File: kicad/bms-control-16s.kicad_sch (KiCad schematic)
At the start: 39 parts, among them J1 MicroFit 2x7, J10 Conn_01x06, J2 UEXT, J3 USB_B_Micro, J4 Conn_01x06, J5 MicroFit 2x9, J9 Conn_01x06

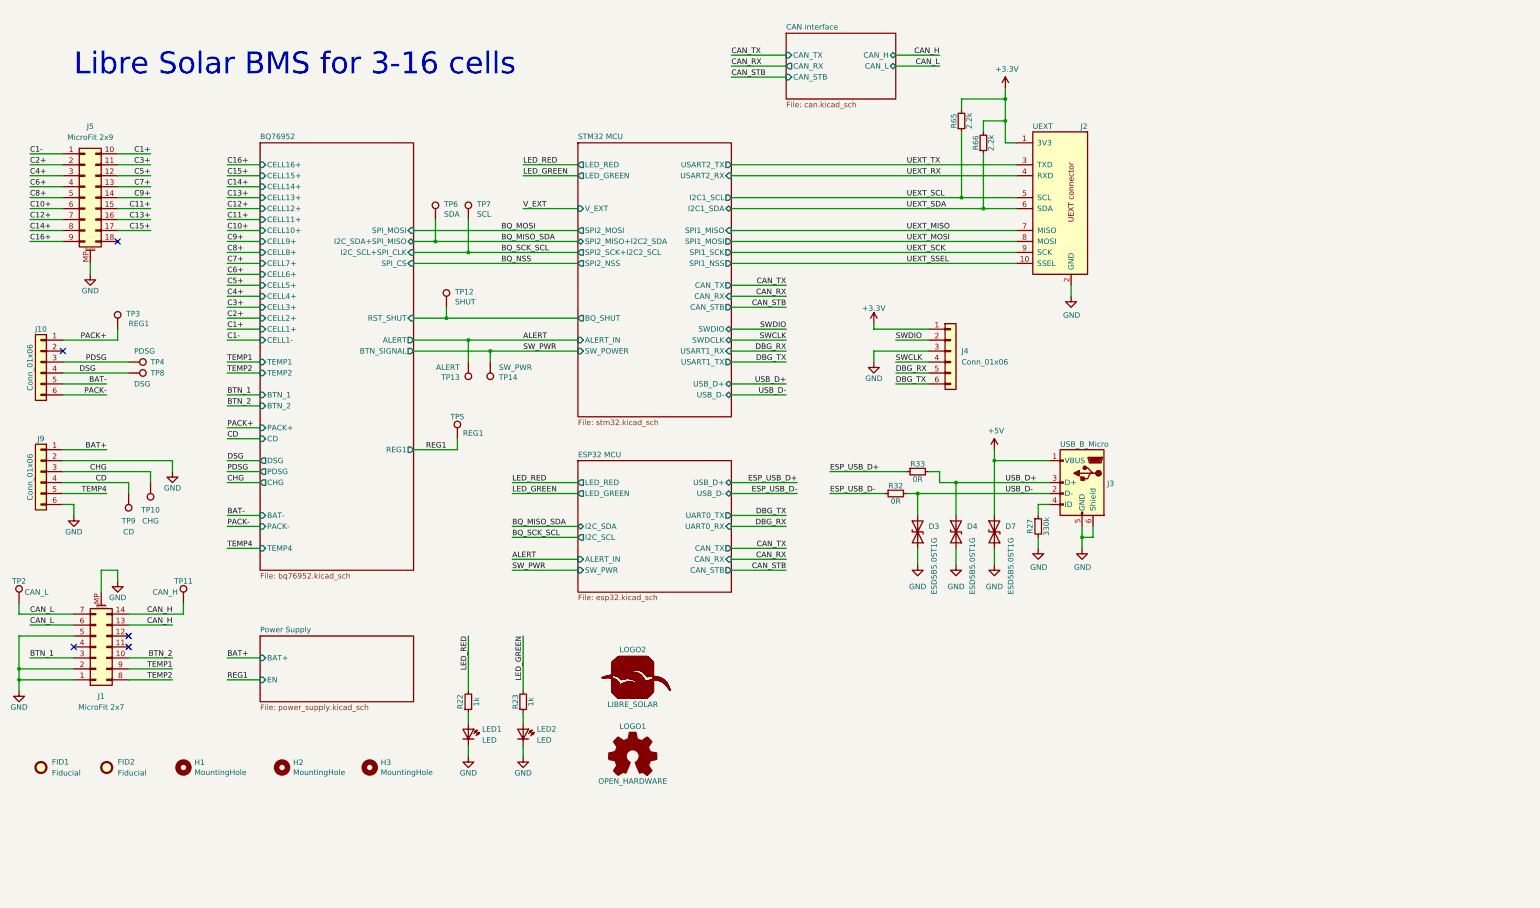
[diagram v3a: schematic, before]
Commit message: Updates based on review comments (v0.2)
This is the design revision that was ordered for the first prototype build.

The pinout of the cell connector and the board-to-board connector changed
compared to v0.1, hence it got a minor revision update.

The control board is now a 4-layer board to improve the grounding of the
PCB. Various other suggested improvements from the design review are also
included in this update.

Fixes #11, #12, #13, #17, #18, #19
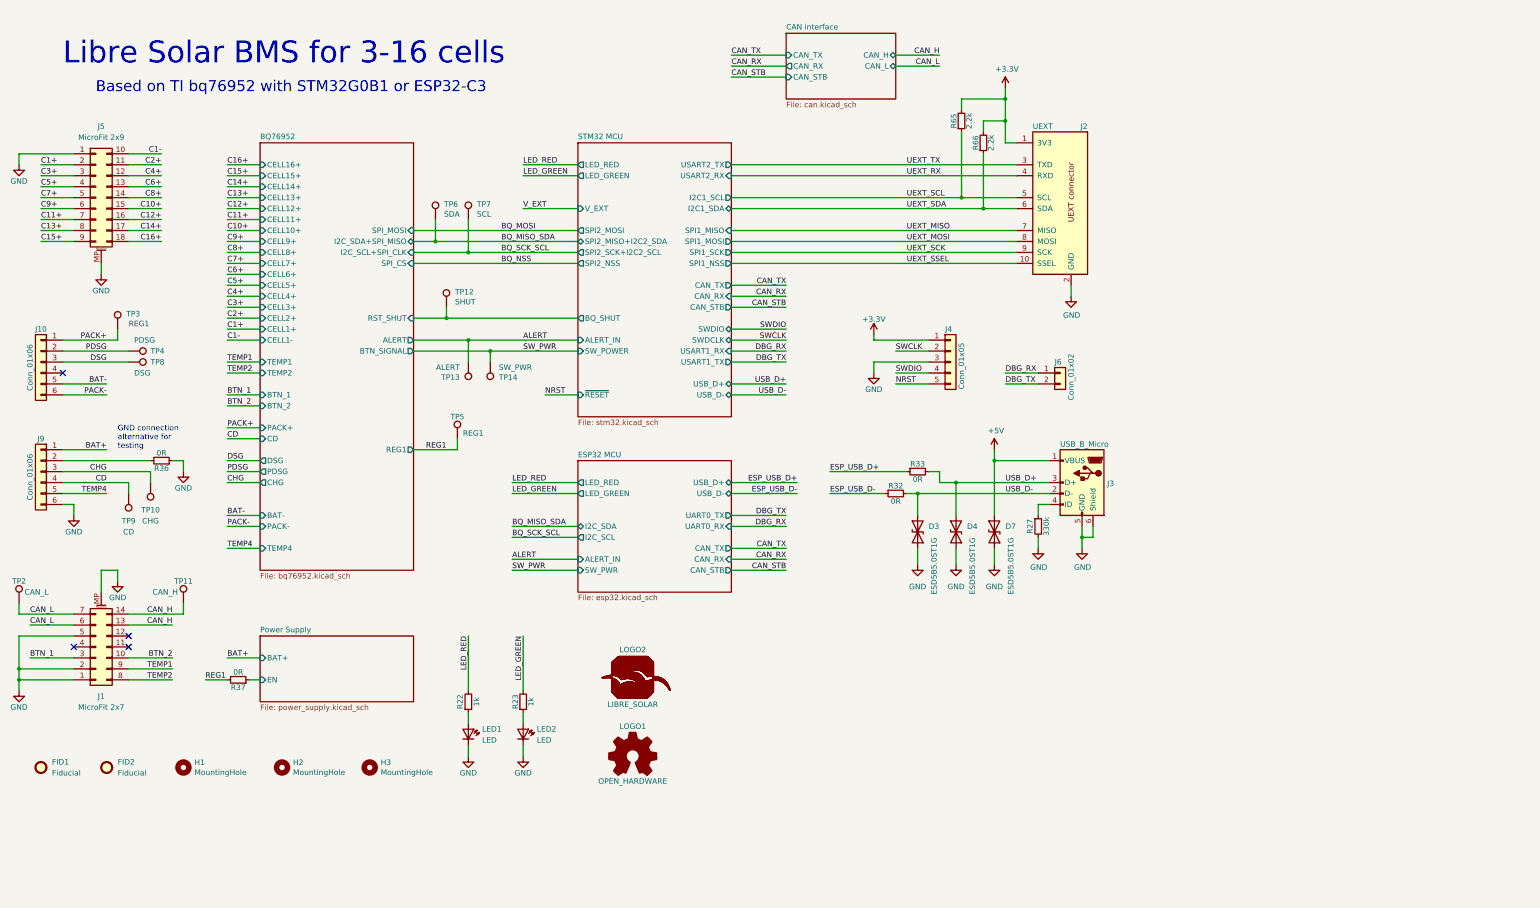
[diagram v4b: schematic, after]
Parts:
- removed J4: Conn_01x06, LibreSolar:Wuerth_WR-WST_2x03_P2.54_DBG, symbol Connector_Generic:Conn_01x06
- added J4: Conn_01x05, Connector_PinHeader_2.54mm:PinHeader_1x05_P2.54mm_Vertical, symbol Connector_Generic:Conn_01x05
- added J6: Conn_01x02, Connector_PinHeader_2.54mm:PinHeader_1x02_P2.54mm_Vertical, symbol Connector_Generic:Conn_01x02
- added R36, R37: 0R, LibreSolar:R_0603_1608, symbol LibreSolar:R
- J1: Manufacturer (none) -> Molex; PartNumber (none) -> 43045-1410; Remarks (none) -> Alternative: Würth 662014231722, 662114231722, mating conne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
- J2: Remarks (none) -> Alternative: any 2x5 box header
- J5: Manufacturer (none) -> Molex; PartNumber (none) -> 43045-1810; Remarks (none) -> Alternative: Würth 662018231722, 662118231722, mating conne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
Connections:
- net +3V3: now also J4.1 (Pin_1)
- net C1+: now also J5.2 (Pin_2); no longer J5.10 (Pin_10)
- net C1-: now also J5.10 (Pin_10); no longer J5.1 (Pin_1)
- net C10+: now also J5.15 (Pin_15); no longer J5.6 (Pin_6)
- net C11+: now also J5.7 (Pin_7); no longer J5.15 (Pin_15)
- net C12+: now also J5.16 (Pin_16); no longer J5.7 (Pin_7)
- net C13+: now also J5.8 (Pin_8); no longer J5.16 (Pin_16)
- net C14+: now also J5.17 (Pin_17); no longer J5.8 (Pin_8)
- net C15+: now also J5.9 (Pin_9); no longer J5.17 (Pin_17)
- net C16+: now also J5.18 (Pin_18); no longer J5.9 (Pin_9)
- net C2+: now also J5.11 (Pin_11); no longer J5.2 (Pin_2)
- net C3+: now also J5.3 (Pin_3); no longer J5.11 (Pin_11)
- net C4+: now also J5.12 (Pin_12); no longer J5.3 (Pin_3)
- net C5+: now also J5.4 (Pin_4); no longer J5.12 (Pin_12)
- net C6+: now also J5.13 (Pin_13); no longer J5.4 (Pin_4)
- net C7+: now also J5.5 (Pin_5); no longer J5.13 (Pin_13)
- net C8+: now also J5.14 (Pin_14); no longer J5.5 (Pin_5)
- net C9+: now also J5.6 (Pin_6); no longer J5.14 (Pin_14)
- net DBG_RX: now also J6.1 (Pin_1)
- net DBG_TX: now also J6.2 (Pin_2)
- net DSG: now also J10.3 (Pin_3); no longer J10.4 (Pin_4)
- net GND: now also J5.1 (Pin_1), J4.3 (Pin_3), R36.1; no longer J9.2 (Pin_2)
- net PDSG: now also J10.2 (Pin_2); no longer J10.3 (Pin_3)
- net REG1: now also R37.2
- net SWCLK: now also J4.2 (Pin_2)
- net SWDIO: now also J4.4 (Pin_4)
- new net: J9.2 (Pin_2), R36.2
- new net NRST: J4.5 (Pin_5)
- new net Power Supply/EN: R37.1
- no-connect marks 5 -> 4
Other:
- sheet STM32 MCU ports: added ~{RESET}; removed none
- note added: "Based on TI bq76952 with STM32G0B1 or ESP32-C3"
- note added: "GND connection alternative for testing"
- moved on the sheet: J5, TP4, TP8
